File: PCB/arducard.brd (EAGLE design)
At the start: 86.5 x 45.8 mm, 97 parts, among them J1 USB MICRO, J2 microSD, J3 051296-4094, J4 M02PTH, Q1 BSS84, Q10 DMG2301U-7, Q2 BC817-16LT1SMD, Q3 DMG2301U-7, Q4 2N7002, Q5 BSS84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

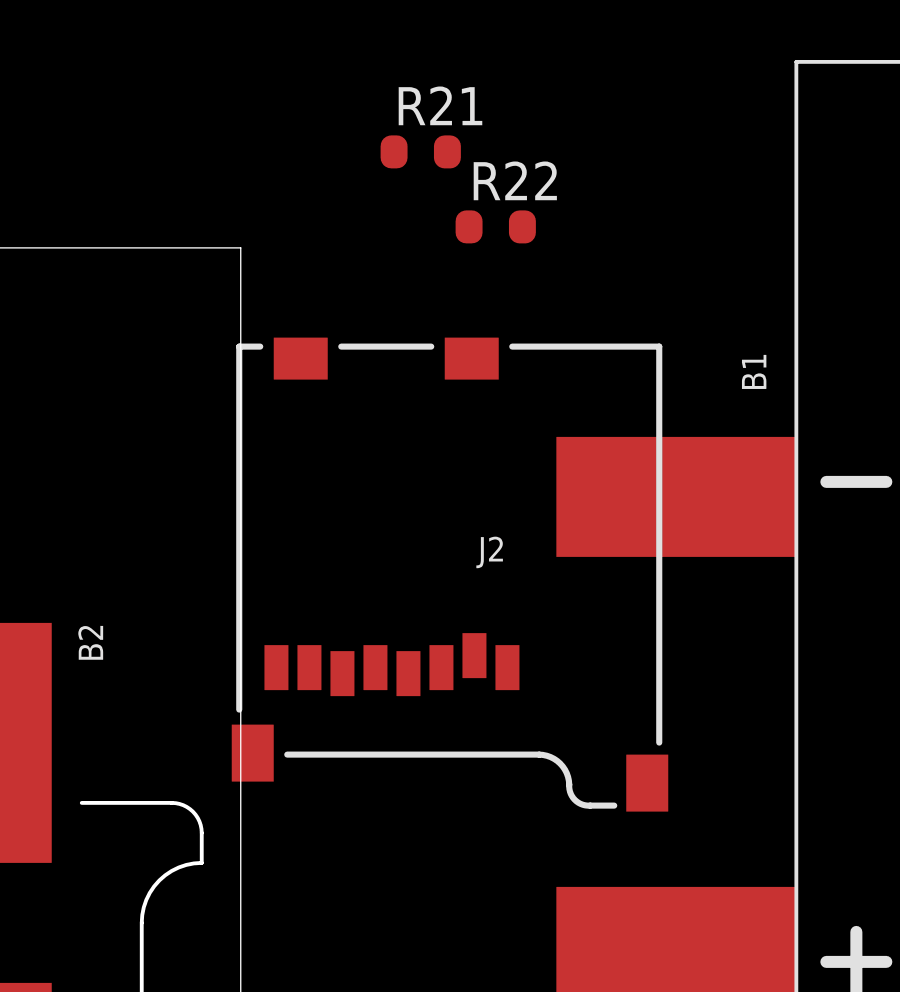
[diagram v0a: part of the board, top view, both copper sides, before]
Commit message: removed microsd
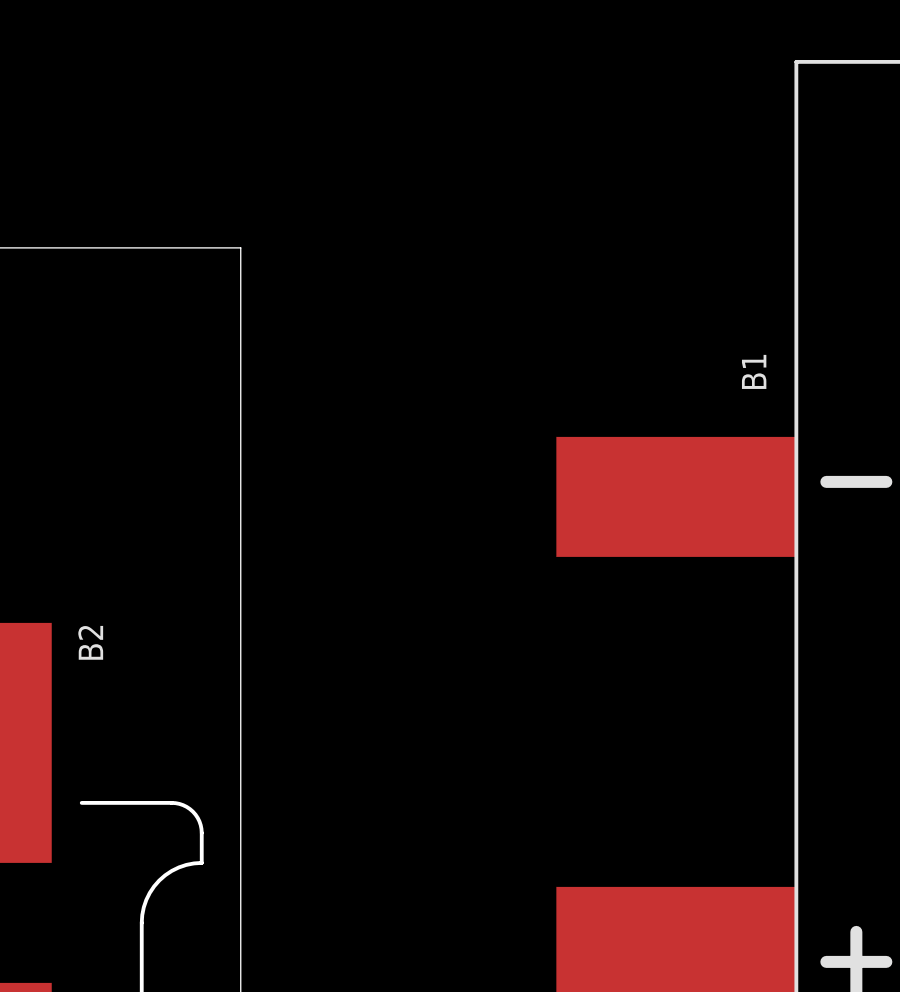
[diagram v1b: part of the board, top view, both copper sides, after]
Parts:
- removed J2: microSD, SparkFun:MICRO-SD-SOCKET-PP
- removed R21: 10k, SmartPrj:R0603-ROUND
- removed R22: 150, SmartPrj:R0603-ROUND
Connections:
- removed net CDP: J2.CD2, R21.1, R22.1
- net +3V3: no longer J2.4, R21.2
- net GND: no longer J2.6, J2.GND1, J2.GND2
- net MISO: no longer J2.7
- net MOSI: no longer J2.3
- net SCK: no longer J2.5
- net SD_CD: no longer R22.2
- net SD_CS: no longer J2.2

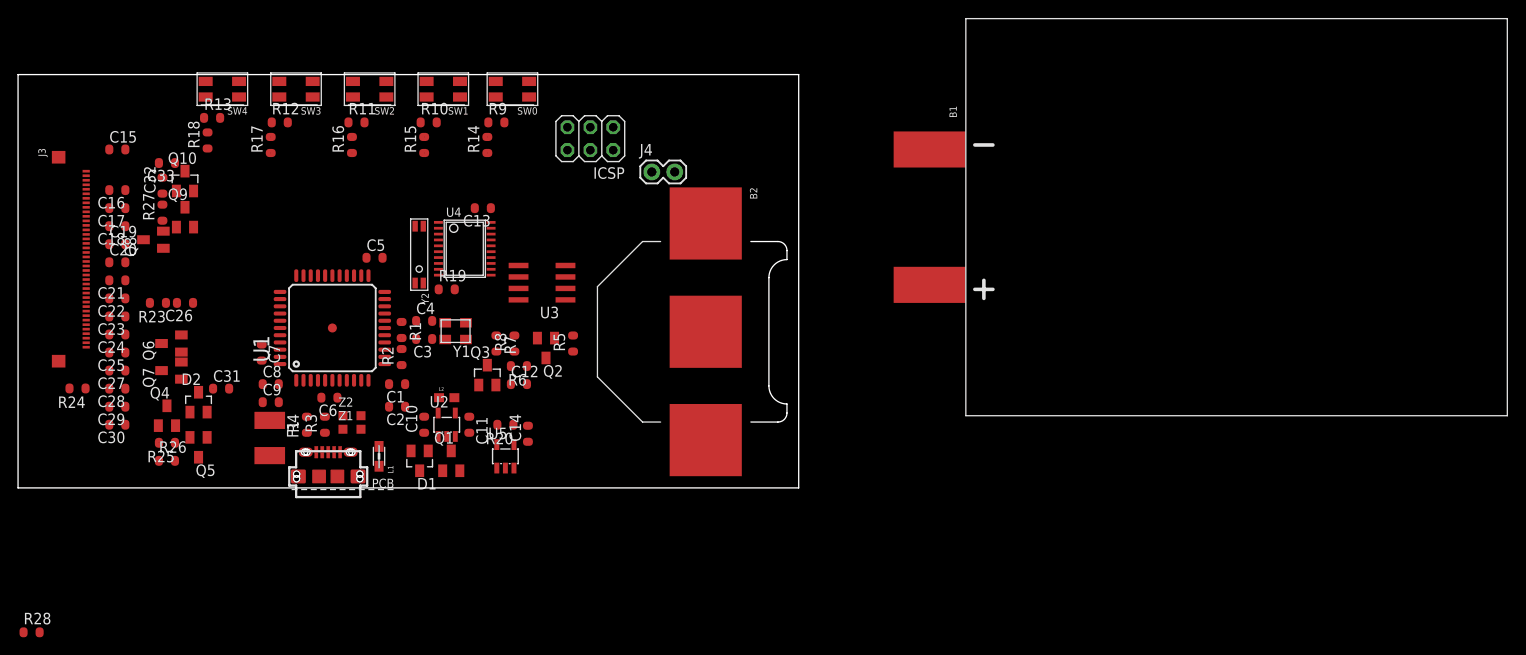
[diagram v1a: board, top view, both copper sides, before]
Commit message: fixed VUSB diode
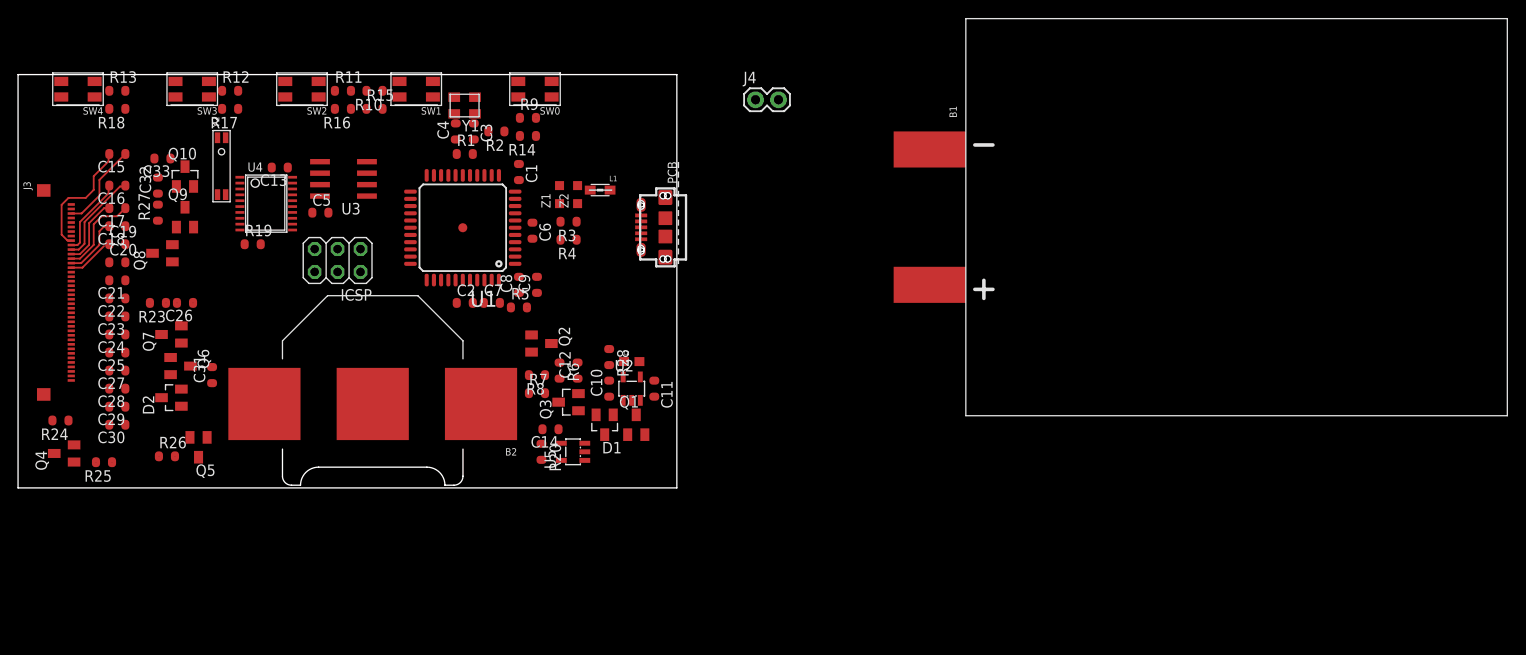
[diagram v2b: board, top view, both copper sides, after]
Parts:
- removed F1: MF-MSMF050-2 500mA, rcl:L1812
- moved R28 70.9 mm to (65.5, 14.5), turned to 270 degrees
- moved J1 46.4 mm to (71.7, 28.9), turned to 90 degrees
- moved L1 38.3 mm to (64.5, 33.0), turned to 180 degrees
- moved B2 37.8 mm to (39.3, 9.30), turned to 180 degrees
- moved R4 35.5 mm to (61.0, 27.5), turned to 180 degrees
- moved R3 35.1 mm to (61.0, 29.5), turned to 180 degrees
- moved Z2 35.0 mm to (62.0, 32.5), turned to 90 degrees
- moved Z1 34.7 mm to (60.0, 32.5), turned to 90 degrees
- moved C9 32.2 mm to (57.5, 22.5), turned to 90 degrees
- moved ICSP 31.1 mm to (35.4, 25.2)
- moved C8 29.6 mm to (55.5, 22.5), turned to 90 degrees
- moved C6 29.1 mm to (57.0, 28.5), turned to 270 degrees
- moved R2 27.1 mm to (53.0, 39.5), turned to 180 degrees
- moved C1 27.1 mm to (55.5, 35.0), turned to 270 degrees
- moved C7 26.1 mm to (52.5, 20.5), turned to 0 degrees
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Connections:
- removed net SCLK: U4.14
- removed net XUSB: F1.2, J1.P1
- net N$10: now also C10.1, Q1.2, U2.1, U2.3
- net SCK: now also U4.14
- net VUSB: now also J1.P1; no longer C10.1, F1.1, Q1.2, U2.1, U2.3
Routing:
- net N$1: track 0.00 -> 13.6 mm
- net N$14: track 0.00 -> 10.3 mm
- net GND: track 0.00 -> 9.74 mm
- net N$16: track 0.00 -> 9.65 mm
- net N$12: track 0.00 -> 8.74 mm
- net N$15: track 0.00 -> 7.74 mm
- net N$18: track 0.00 -> 6.80 mm
- net N$19: track 0.00 -> 4.62 mm
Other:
- board size 86.5 x 45.8 mm -> 73 x 45.8 mm

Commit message: removed flat cell battery connector
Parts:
- removed B1: PGEB016144, arducard-battery:PGEB014461
- removed J4: M02PTH, SparkFun-Connectors:1X02
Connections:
- new net XUSB: J1.P1
- net BATT_RAW: no longer B1.+, J4.1
- net GND: no longer B1.-, J4.2
- net VUSB: no longer J1.P1
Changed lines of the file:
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@@
 <element name="Q3" library="transistor-fet" package="SOT23" value="DMG2301U-7" x="61" y="9.5" rot="R90"/>
 <element name="R20" library="SmartPrj" package="R0603-ROUND" value="18.2k" x="58" y="4" rot="R270"/>
-<element name="J4" library="SparkFun-Connectors" package="1X02" value="M02PTH" x="81.72" y="43.01"/>
 <element name="C8" library="SmartPrj" package="C0603-ROUND" value="10u" x="55.5" y="22.5" rot="R90"/>
 <element name="R2" library="SmartPrj" package="R0603-ROUND" value="10k" x="53" y="39.5" rot="R180"/>
@@
 <attribute name="OC_FARNELL" value="unknown" x="165.79" y="-75.36" size="1.778" layer="27" display="off"/>
 </element>
-<element name="B1" library="arducard-battery" package="PGEB014461" value="PGEB016144" x="105.02" y="8"/>
 <element name="B2" library="arducard-coincell" package="BK-5067" value="LIR2016" x="39.3" y="9.3" rot="R180"/>
 <element name="R28" library="SmartPrj" package="R0603-ROUND" value="10k" x="65.5" y="14.5" rot="R270"/>
@@
 <contactref element="C14" pad="2"/>
 <contactref element="U5" pad="2"/>
-<contactref element="B1" pad="-"/>
-<contactref element="J4" pad="2"/>
 <contactref element="U1" pad="15"/>
 <contactref element="U1" pad="23"/>
@@
 <contactref element="C13" pad="2"/>
 <contactref element="R28" pad="1"/>
-<wire x1="84.26" y1="43.01" x2="101.02" y2="37.5" width="0" layer="19" extent="1-1"/>
-<wire x1="71.73" y1="32.172" x2="84.26" y2="43.01" width="0" layer="19" extent="1-1"/>
+<wire x1="5.899" y1="30.407" x2="7.039" y2="30.407" width="0.2032" layer="1"/>
+<wire x1="7.039" y1="30.407" x2="9.017" y2="32.385" width="0.2032" layer="1"/>
+<wire x1="9.017" y1="32.385" x2="9.017" y2="34.128" width="0.2032" layer="1"/>
+<wire x1="9.017" y1="34.128" x2="11.889" y2="37" width="0.2032" layer="1"/>
 <wire x1="71.73" y1="29.886" x2="71.73" y2="32.172" width="0" layer="19" extent="1-1"/>
 <wire x1="71.73" y1="27.854" x2="71.73" y2="29.886" width="0" layer="19" extent="1-1"/>
@@
 <wire x1="24.5822" y1="28.575" x2="28.111" y2="35.5" width="0" layer="19" extent="1-1"/>
 <wire x1="17.1" y1="26.95" x2="24.5822" y2="28.575" width="0" layer="19" extent="1-1"/>
-<wire x1="15.5" y1="34.389" x2="17.1" y2="26.95" width="0" layer="19" extent="1-1"/>
-<wire x1="15.111" y1="36.5" x2="15.5" y2="34.389" width="0" layer="19" extent="1-1"/>
-<wire x1="11.889" y1="37" x2="15.111" y2="36.5" width="0" layer="19" extent="1-1"/>
-<wire x1="11.889" y1="44" x2="11.889" y2="37" width="0" layer="19" extent="1-1"/>
 <wire x1="19.389" y1="20.5" x2="17.1" y2="26.95" width="0" layer="19" extent="1-1"/>
 <wire x1="18.1" y1="17.95" x2="19.389" y2="20.5" width="0" layer="19" extent="1-1"/>
@@
 <wire x1="11.889" y1="7" x2="11.889" y2="9" width="0" layer="19" extent="1-1"/>
 <wire x1="5.899" y1="15.407" x2="11.889" y2="13" width="0" layer="19" extent="1-1"/>
+<wire x1="15.5" y1="34.389" x2="17.1" y2="26.95" width="0" layer="19" extent="1-1"/>
+<wire x1="15.111" y1="36.5" x2="15.5" y2="34.389" width="0" layer="19" extent="1-1"/>
+<wire x1="11.889" y1="37" x2="15.111" y2="36.5" width="0" layer="19" extent="1-1"/>
+<wire x1="11.889" y1="44" x2="11.889" y2="37" width="0" layer="19" extent="1-1"/>
 <wire x1="24.389" y1="44" x2="28.111" y2="35.5" width="0" layer="19" extent="1-1"/>
 <wire x1="39.3" y1="9.3" x2="46.08" y2="23.03" width="0" layer="19" extent="1-1"/>
-<wire x1="5.899" y1="30.407" x2="7.039" y2="30.407" width="0.2032" layer="1"/>
-<wire x1="7.039" y1="30.407" x2="9.017" y2="32.385" width="0.2032" layer="1"/>
-<wire x1="9.017" y1="32.385" x2="9.017" y2="34.128" width="0.2032" layer="1"/>
-<wire x1="9.017" y1="34.128" x2="11.889" y2="37" width="0.2032" layer="1"/>
 </signal>
 <signal name="RESET">
@@
 <wire x1="55.08" y1="27.23" x2="60.111" y2="29.5" width="0" layer="19" extent="1-1"/>
 </signal>
-<signal name="VUSB" class="3">
+<signal name="VUSB">
 <contactref element="U1" pad="7"/>
 <contactref element="C9" pad="2"/>
@@
 <contactref element="R28" pad="2"/>
 <contactref element="D1" pad="1"/>
-<contactref element="J1" pad="P1"/>
-<wire x1="57.5" y1="23.389" x2="69.0376" y2="27.5492" width="0" layer="19" extent="1-1"/>
-<wire x1="55.5" y1="23.389" x2="57.5" y2="23.389" width="0" layer="19" extent="1-1"/>
-<wire x1="55.08" y1="29.63" x2="55.5" y2="23.389" width="0" layer="19" extent="1-1"/>
+<wire x1="55.5" y1="23.389" x2="55.08" y2="29.63" width="0" layer="19" extent="1-1"/>
+<wire x1="57.5" y1="23.389" x2="55.5" y2="23.389" width="0" layer="19" extent="1-1"/>
 <wire x1="65.5" y1="13.611" x2="57.5" y2="23.389" width="0" layer="19" extent="1-1"/>
 <wire x1="65.95" y1="8.1" x2="65.5" y2="13.611" width="0" layer="19" extent="1-1"/>
@@
 <wire x1="61.889" y1="29.5" x2="69.0376" y2="28.87" width="0" layer="19" extent="1-1"/>
 <wire x1="60" y1="31.5" x2="61.889" y2="29.5" width="0" layer="19" extent="1-1"/>
+</signal>
+<signal name="XUSB" class="3">
+<contactref element="J1" pad="P1"/>
 </signal>
 <signal name="USBID">
@@
 <contactref element="Q3" pad="2"/>
 <contactref element="U5" pad="3"/>
-<contactref element="B1" pad="+"/>
-<contactref element="J4" pad="1"/>
 <contactref element="B2" pad="POS1"/>
 <contactref element="B2" pad="POS2"/>
 <contactref element="Q1" pad="3"/>
-<wire x1="101.02" y1="22.5" x2="81.72" y2="43.01" width="0" layer="19" extent="1-1"/>
-<wire x1="68.5" y1="8.1" x2="101.02" y2="22.5" width="0" layer="19" extent="1-1"/>
 <wire x1="62.8" y1="4.95" x2="68.5" y2="8.1" width="0" layer="19" extent="1-1"/>
 <wire x1="62.1" y1="10.45" x2="62.8" y2="4.95" width="0" layer="19" extent="1-1"/>

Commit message: initial routing for dorkbot
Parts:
- removed L1: MH2029-300Y, wuerth-elektronik:0805
- moved SW0 44.4 mm to (72.5, 2.43), turned to 0 degrees
- moved R10 43.9 mm to (51.9, 1.85), turned to 0 degrees
- moved SW1 43.8 mm to (57.2, 2.43), turned to 0 degrees
- moved SW2 43.0 mm to (41.9, 2.43), turned to 0 degrees
- moved R13 42.9 mm to (6.47, 1.34), turned to 180 degrees
- moved R11 42.5 mm to (35.5, 1.47), turned to 180 degrees
- moved R25 42.4 mm to (20.7, 43.8), turned to 0 degrees
- moved SW3 42.4 mm to (26.6, 2.43), turned to 0 degrees
- moved R12 42.3 mm to (21.7, 1.73), turned to 180 degrees
- moved SW4 42.0 mm to (11.3, 2.43), turned to 0 degrees
- moved R20 41.8 mm to (74.0, 42.6), turned to 180 degrees
- moved R15 40.1 mm to (51.9, 3.85), turned to 180 degrees
- moved R9 40.1 mm to (66.9, 2.31), turned to 180 degrees
- moved R18 38.9 mm to (6.47, 3.34), turned to 0 degrees
- moved Q4 38.8 mm to (20.8, 39.3), turned to 0 degrees
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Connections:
- removed net N$10: C10.1, D1.3, Q1.2, U2.1, U2.3
- removed net XUSB: J1.P1
- new net 5V: C10.1, C14.1, D1.3, Q1.2, U1.7, U2.1, U2.3, U5.4
- net GND: no longer L1.1, L1.2
- net VUSB: now also J1.P1; no longer C14.1, U1.7, U5.4
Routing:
- net GND: track 9.74 -> 355.5 mm, vias 0 -> 9
- net +3V3: track 0.00 -> 204.0 mm, vias 0 -> 7
- net MOSI: track 0.00 -> 100.5 mm, vias 0 -> 3
- net SCK: track 0.00 -> 85.9 mm, vias 0 -> 5
- net MISO: track 0.00 -> 72.6 mm, vias 0 -> 3
- net DISCHARGE: track 0.00 -> 70.8 mm, vias 0 -> 2
- net PWM: track 0.00 -> 63.2 mm, vias 0 -> 2
- net BORDER_CONTROL: track 0.00 -> 59.2 mm, vias 0 -> 4
- net 5V: track 0.00 -> 59.2 mm, vias 0 -> 3
- net BATT_RAW: track 0.00 -> 56.7 mm
- net B4: track 0.00 -> 56.6 mm, vias 0 -> 2
- net VCC_T: track 0.00 -> 56.0 mm, vias 0 -> 3
- net VUSB: track 0.00 -> 53.6 mm, vias 0 -> 5
- net B3: track 0.00 -> 53.4 mm, vias 0 -> 4
- net B2: track 0.00 -> 50.8 mm, vias 0 -> 4
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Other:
- board size 73 x 45.8 mm -> 82.3 x 45.8 mm
